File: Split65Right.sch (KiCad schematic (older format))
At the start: 89 parts, among them J1 Jack4, J2 OLED, SW1 SW_PUSH, SW10 SW_PUSH, SW11 SW_PUSH, SW12 SW_PUSH, SW13 SW_PUSH, SW14 SW_PUSH, SW15 SW_PUSH, SW16 SW_PUSH, SW17 SW_PUSH, SW18 SW_PUSH, SW19 SW_PUSH, SW2 SW_PUSH, SW20 SW_PUSH, SW21 SW_PUSH, SW22 SW_PUSH, SW23 SW_PUSH, SW24 SW_PUSH, SW25 SW_PUSH, SW26 SW_PUSH, SW27 SW_PUSH, SW28 SW_PUSH, SW29 SW_PUSH, SW3 SW_PUSH, SW30 SW_PUSH, SW31 SW_PUSH, SW32 SW_PUSH, SW33 SW_PUSH, SW34 SW_PUSH, SW35 SW_PUSH, SW36 SW_PUSH, SW37 SW_PUSH, SW38 SW_PUSH, SW39 SW_PUSH, SW4 SW_PUSH, SW40 SW_PUSH, SW5 SW_PUSH, SW6 SW_PUSH, SW7 SW_PUSH, SW8 SW_PUSH, SW9 SW_PUSH, U1 proton_c

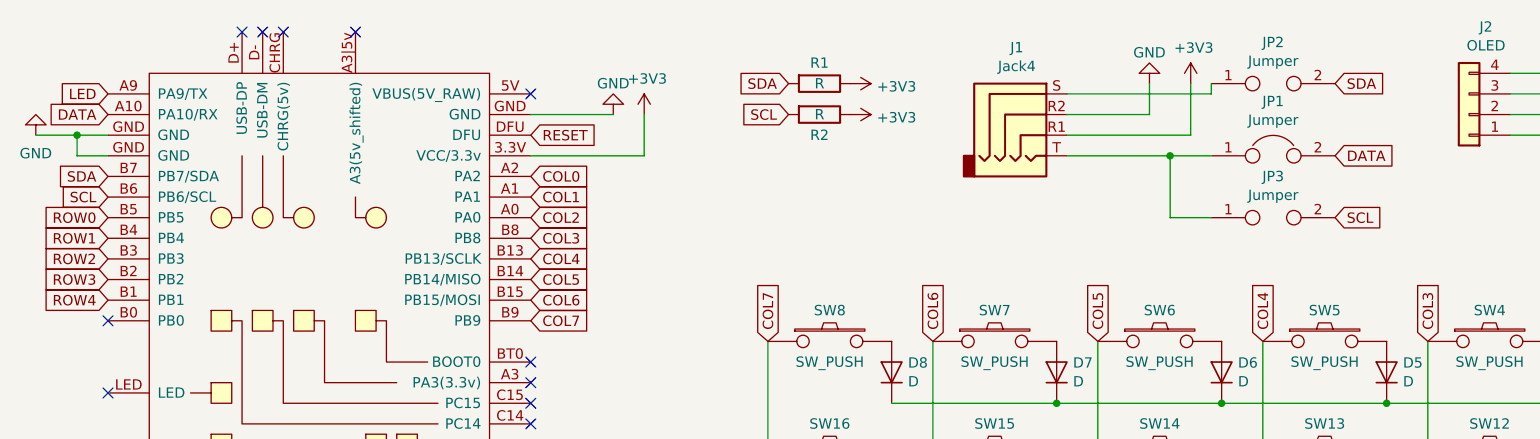
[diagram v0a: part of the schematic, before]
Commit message: modified:   Split65Left-cache.lib 	modified:   Split65Left.kicad_pcb 	modified:   Split65Left.kicad_pcb-bak 	modified:   Split65Left.net 	modified:   Split65Left.sch 	modified:   Split65Left.sch-bak 	modified:   Split65Right-cache.lib 	modified:   Split65Right.kicad_pcb 	modified:   Split65Right.kicad_pcb-bak 	modified:   Split65Right.net 	modified:   Split65Right.sch 	modified:   Split65Right.sch-bak
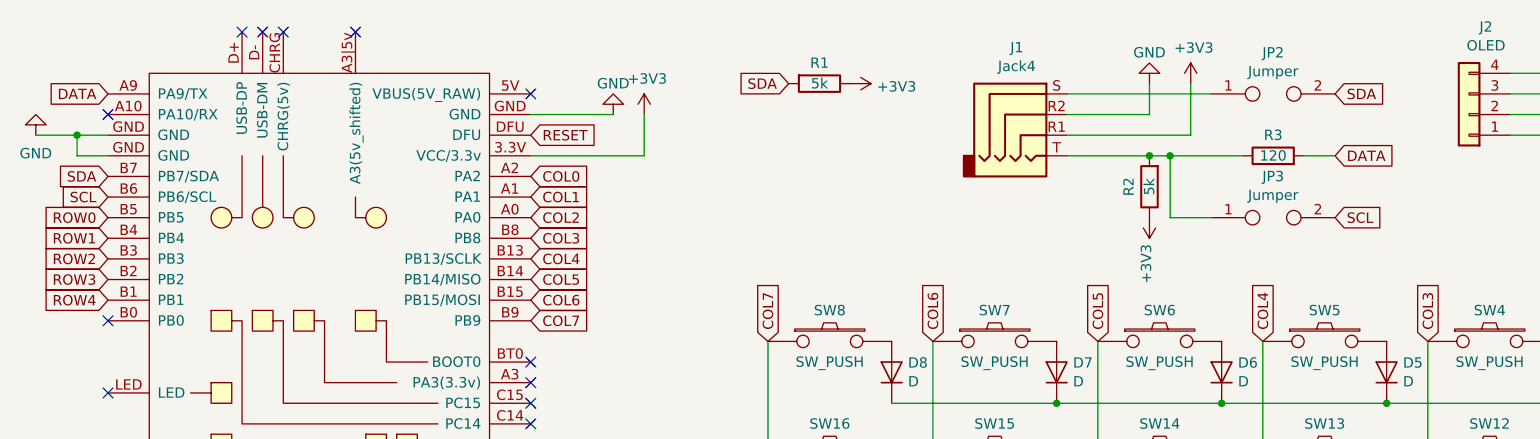
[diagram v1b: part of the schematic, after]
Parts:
- removed JP1: Jumper, footprints:jumper_data, symbol Device:Jumper
- added R3: 120, footprints:R_1608_axial, symbol Device:R
- R1, R2: value R -> 5k
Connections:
- net LED is gone; now on net DATA: U1.A9 (PA9/TX)
- net DATA: now also R3.2; no longer U1.A10 (PA10/RX)
- net SCL: no longer R2.2
- net at J1.T, JP3.1: now also R2.2, R3.1
- no-connect marks 23 -> 24
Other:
- moved on the sheet: JP2, R2
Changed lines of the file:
@@
 Wire Wire Line
 	1050 1500 850  1500
-Text GLabel 1200 1400 0    50   Input ~ 0
+Text GLabel 1200 1300 0    50   Input ~ 0
 DATA
-Text GLabel 1200 1300 0    50   Input ~ 0
-LED
 Text GLabel 1200 1700 0    50   Input ~ 0
 SDA
@@
 Text GLabel 4500 1250 0    50   Input ~ 0
 SDA
-Text GLabel 4500 1400 0    50   Input ~ 0
-SCL
 $Comp
 L Device:R R1
@@
 P 4650 1250
 F 0 "R1" V 4550 1250 50  0000 C CNN
-F 1 "R" V 4650 1250 50  0000 C CNN
+F 1 "5k" V 4650 1250 50  0000 C CNN
 F 2 "footprints:R_1608_axial" V 4580 1250 50  0001 C CNN
 F 3 "~" H 4650 1250 50  0001 C CNN
@@
 L Device:R R2
 U 1 1 5F79541D
-P 4650 1400
-F 0 "R2" V 4750 1400 50  0000 C CNN
-F 1 "R" V 4650 1400 50  0000 C CNN
-F 2 "footprints:R_1608_axial" V 4580 1400 50  0001 C CNN
-F 3 "~" H 4650 1400 50  0001 C CNN
-	1    4650 1400
-	0    1    1    0
+P 6250 1750
+F 0 "R2" V 6350 1750 50  0000 C CNN
+F 1 "5k" V 6250 1750 50  0000 C CNN
+F 2 "footprints:R_1608_axial" V 6180 1750 50  0001 C CNN
+F 3 "~" H 6250 1750 50  0001 C CNN
+	1    6250 1750
+	-1   0    0    1
 $EndComp
 $Comp
@@
 L power:+3V3 #PWR0105
 U 1 1 5F796502
-P 4800 1400
-F 0 "#PWR0105" H 4800 1250 50  0001 C CNN
-F 1 "+3V3" V 4815 1528 50  0000 L CNN
-F 2 "" H 4800 1400 50  0001 C CNN
-F 3 "" H 4800 1400 50  0001 C CNN
-	1    4800 1400
-	0    1    1    0
+P 6250 1900
+F 0 "#PWR0105" H 6250 1750 50  0001 C CNN
+F 1 "+3V3" V 6265 2028 50  0000 L CNN
+F 2 "" H 6250 1900 50  0001 C CNN
+F 3 "" H 6250 1900 50  0001 C CNN
+	1    6250 1900
+	-1   0    0    1
 $EndComp
 $Comp
@@
 	1    0    0    -1
 $EndComp
-$Comp
-L Device:Jumper JP1
-U 1 1 5F79AB96
-P 6850 1600
-F 0 "JP1" H 6850 1864 50  0000 C CNN
-F 1 "Jumper" H 6850 1773 50  0000 C CNN
-F 2 "footprints:jumper_data" H 6850 1600 50  0001 C CNN
-F 3 "~" H 6850 1600 50  0001 C CNN
-	1    6850 1600
-	1    0    0    -1
-$EndComp
 Wire Wire Line
 	5850 1300 6550 1300
 Wire Wire Line
-	6550 1300 6550 1250
-Wire Wire Line
-	5850 1600 6350 1600
+	5850 1600 6250 1600
 Wire Wire Line
 	6550 1900 6350 1900
@@
 	6350 1900 6350 1600
 Connection ~ 6350 1600
-Wire Wire Line
-	6350 1600 6550 1600
 Text GLabel 7150 1600 2    50   Input ~ 0
 DATA
-Text GLabel 7150 1250 2    50   Input ~ 0
+Text GLabel 7150 1300 2    50   Input ~ 0
 SDA
 Text GLabel 7150 1900 2    50   Input ~ 0
@@
 L keyboard_parts:Jumper JP2
 U 1 1 5F78F78F
-P 6850 1250
-F 0 "JP2" H 6850 1450 50  0000 C CNN
-F 1 "Jumper" H 6850 1359 50  0000 C CNN
-F 2 "footprints:Jumper" H 6850 1250 50  0001 C CNN
-F 3 "" H 6850 1250 50  0001 C CNN
-	1    6850 1250
+P 6850 1300
+F 0 "JP2" H 6850 1500 50  0000 C CNN
+F 1 "Jumper" H 6850 1409 50  0000 C CNN
+F 2 "footprints:Jumper" H 6850 1300 50  0001 C CNN
+F 3 "" H 6850 1300 50  0001 C CNN
+	1    6850 1300
 	1    0    0    -1
 $EndComp
@@
 NoConn ~ 1200 3200
 NoConn ~ 1200 2750
+NoConn ~ 1200 1400
+Connection ~ 6250 1600
+Wire Wire Line
+	6250 1600 6350 1600
+$Comp
+L Device:R R3
+U 1 1 5F7AC61F
+P 6850 1600
+F 0 "R3" V 6950 1600 50  0000 C CNN
+F 1 "120" V 6850 1600 50  0000 C CNN
+F 2 "footprints:R_1608_axial" V 6780 1600 50  0001 C CNN
+F 3 "~" H 6850 1600 50  0001 C CNN
+	1    6850 1600
+	0    -1   -1   0
+$EndComp
+Wire Wire Line
+	7150 1600 7000 1600
+Wire Wire Line
+	6350 1600 6700 1600
 $EndSCHEMATC
